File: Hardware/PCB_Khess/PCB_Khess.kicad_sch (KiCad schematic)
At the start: 13 parts, among them J1 Screw_Terminal_01x02, J2 USB3_A, J3 RJ11_Connector, J4 Conn_01x02, Q1 BUZ11, U1 R-78B5.0-2.0

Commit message: fix: add name pcb
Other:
- title: (none) -> PCB K'Hess
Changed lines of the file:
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@@
 	(generator_version "9.0")
 	(paper "A4")
+	(title_block
+		(title "PCB K'Hess")
+		(rev "1.0")
+	)
 	(rectangle
 		(start 26.67 21.59)

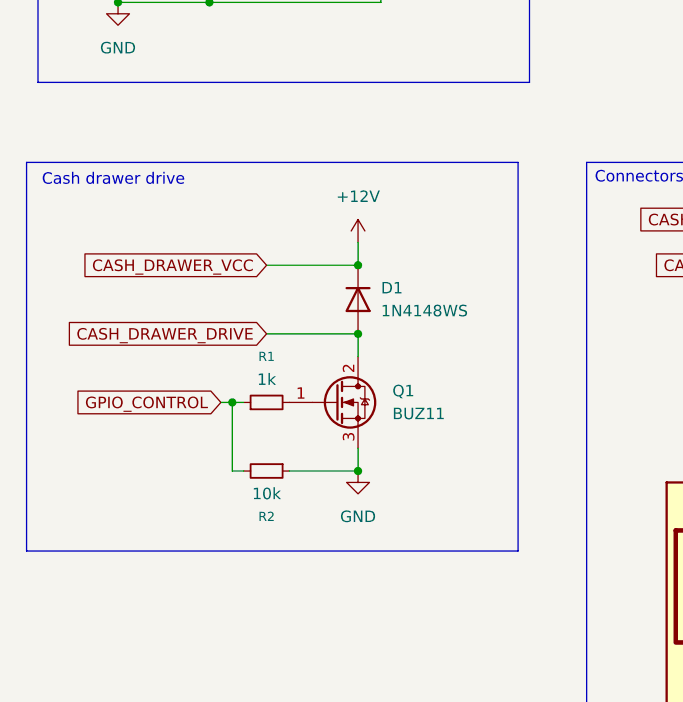
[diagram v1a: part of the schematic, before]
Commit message: feat: update pcb cash register and add datasheet
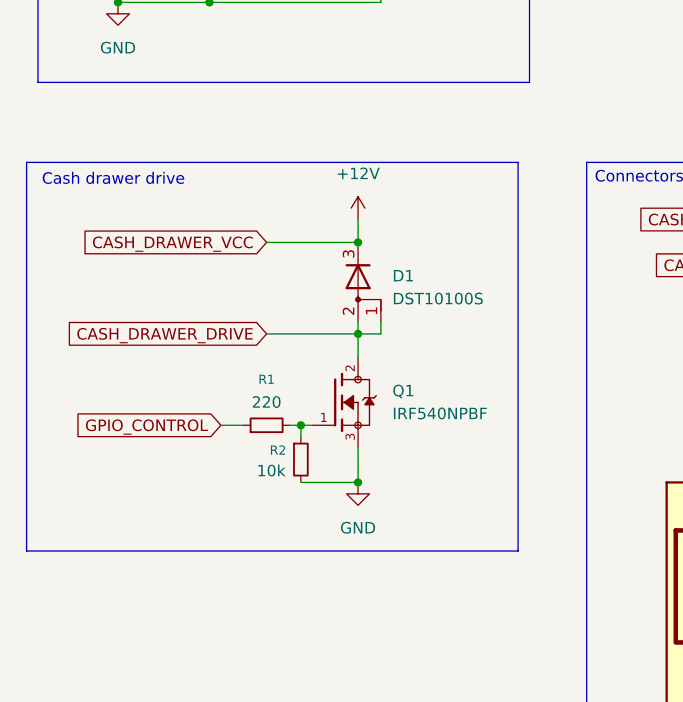
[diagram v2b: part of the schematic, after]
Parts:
- removed D1: 1N4148WS, Diode_SMD:D_SOD-323, symbol Diode:1N4148WS
- removed Q1: BUZ11, Package_TO_SOT_THT:TO-220-3_Vertical, symbol Transistor_FET:BUZ11
- added D1: DST10100S, symbol Device:D_AAK
- added Q1: IRF540NPBF, IRF540NPBF:TO254P1054X469X1930-3, symbol IRF540NPBF:IRF540NPBF
- R1: value 1k -> 220
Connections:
- net +12V: now also D1.3 (K)
- net CASH_DRAWER_DRIVE: now also D1.1 (A), D1.2 (A), Q1.2
- net GND: now also R2.2, Q1.3; no longer R2.1
- net GPIO_CONTROL: no longer R2.2
- net at R1.2: now also R2.1, Q1.1
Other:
- moved on the sheet: R1, R2

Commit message: fix: update pcb main
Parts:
- removed J2: USB3_A, symbol Connector:USB3_A
- removed J4: Conn_01x02, symbol Connector_Generic:Conn_01x02
- removed Q1: IRF540NPBF, IRF540NPBF:TO254P1054X469X1930-3, symbol IRF540NPBF:IRF540NPBF
- added J2: Raspberry_Pi_4, symbol Connector:Raspberry_Pi_4
- added Q1: BUK9637-100E,118, symbol Transistor_FET:Q_NMOS_GDS
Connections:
- net +5V: now also J2.2 (5V), J2.4 (5V)
- net CASH_DRAWER_DRIVE: now also Q1.2 (D)
- net GND: now also J2.14 (GND), J2.20 (GND), J2.25 (GND), J2.30 (GND), J2.34 (GND), J2.39 (GND), J2.6 (GND), J2.9 (GND), Q1.3 (S)
- net GPIO_CONTROL: now also J2.12 (GPIO18/SPI1_~{CE0}/PCM_CLK/PWM0)
- net at R1.2, R2.1: now also Q1.1 (G)
- new net: J2.1 (3V3), J2.17 (3V3)
- no-connect marks 12 -> 32
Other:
- moved on the sheet: C1, C2, D1, J1, J3, L1, R1, R2, U1

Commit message: fix: update pcb
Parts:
- removed J2: Raspberry_Pi_4, symbol Connector:Raspberry_Pi_4
- added J2: Conn_01x02, symbol Connector_Generic:Conn_01x02
- added J4: USB3_A, symbol Connector:USB3_A
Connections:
- net +5V: now also J4.1 (VBUS)
- net GND: now also J2.2 (Pin_2), J4.4 (GND)
- net GPIO_CONTROL: now also J2.1 (Pin_1)
- no-connect marks 32 -> 12

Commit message: fix: update pcb
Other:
- note added: "230V AC to 12V DC Convertor"
- note removed: "AC to 12V DC Convertor"
- moved on the sheet: C1, C2, D1, J1, J2, J3, J4, L1, PS1, Q1, R1, R2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
